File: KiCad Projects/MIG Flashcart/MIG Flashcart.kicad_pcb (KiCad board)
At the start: 4 copper layers, 27.4 x 17 mm, 35 parts, among them J1 Conn_02x04_Counter_Clockwise, J2 Conn_01x17, J3 1040310811, SW1 EVQ-P7A01P, U1 ICE40UP5K-SG48ITR, U2 ESP32-S2, U3 TLV70012_SOT353, U4 TLV70025_SOT353, Y1 ECS-400-10-37B2-CKY-TR

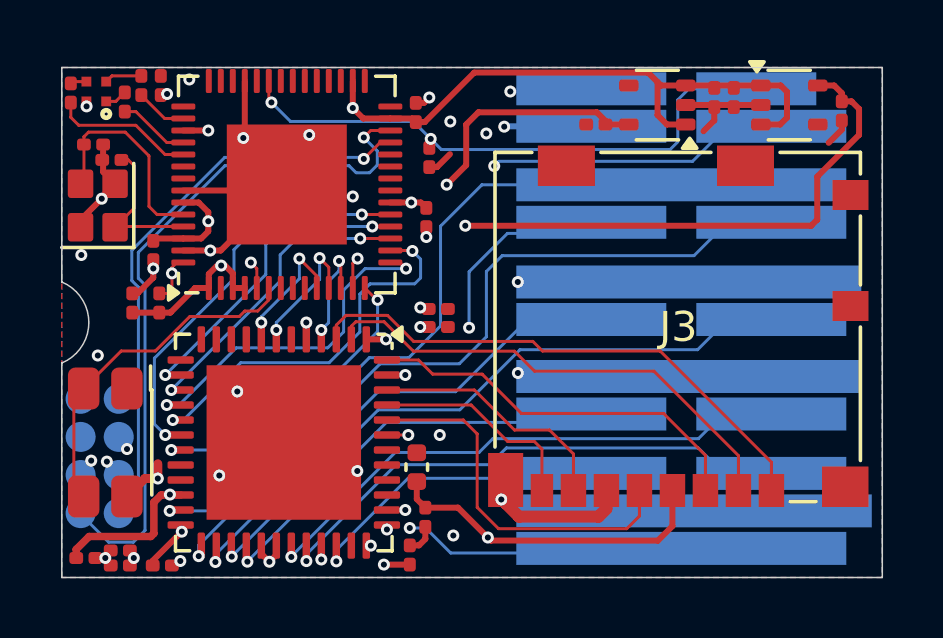
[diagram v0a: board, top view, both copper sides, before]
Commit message: Updated Flashcart PCB, uploaded Flashcart BOM
Revised the Flashcart PCB to the newer revision of the MIG v2, as well as added DigiKey and Mouser BOMs for the Flashcart. One capacitor measurement on the Dumper PCB was corrected as well.
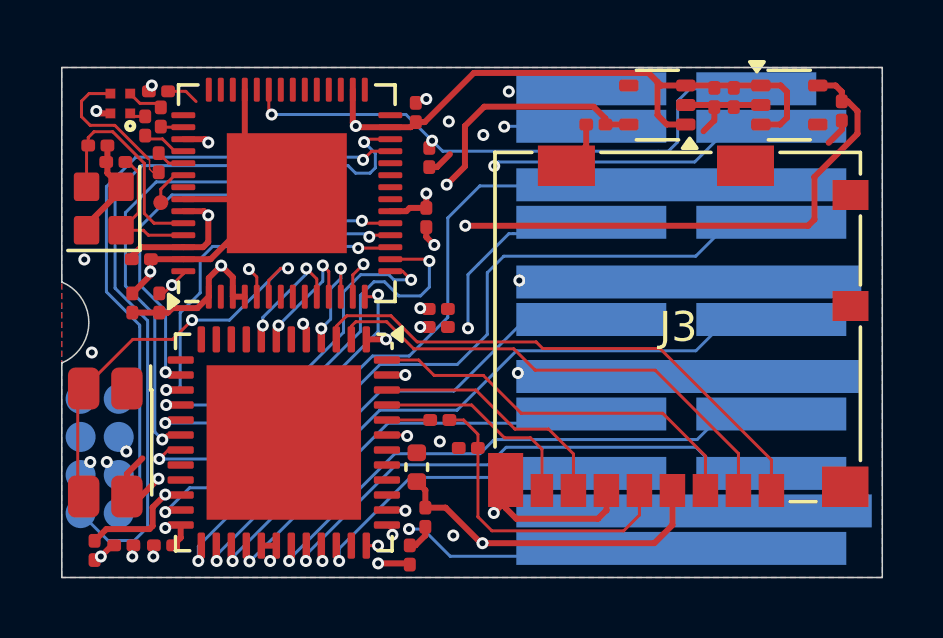
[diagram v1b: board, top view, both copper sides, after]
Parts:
- removed the C5 at (133.9, 112.6)
- added C7: DNP, Capacitor_SMD:C_0201_0603Metric, F.Cu at (145.5, 109.2)
- added R1: 50R, Resistor_SMD:R_0201_0603Metric, F.Cu at (144.6, 108.2)
- added TP1: TestPoint, MIG Flashcart:TestPoint_Pad_D0.5mm, F.Cu at (135.2, 101.0)
- C1, C11, C12, C20, C3, C4, C8, C9: value C -> 0.82u
- C10, C15, C2: value C -> 0.88u
- C16: value 1u -> 0.88u
- C17, C18, C19: value 1u -> 0.82u
- C5: renamed from C6; value C -> 0.82u
- C6: renamed from C7; value C -> 3u3
- moved R3 3.74 mm to (135.2, 99.7), turned to -90 degrees
- moved R6 1.23 mm to (135.2, 98.2)
- moved R5 1.05 mm to (134.7, 98.5)
- moved D1 0.89 mm to (133.9, 97.7)
- moved C2 0.68 mm to (134.0, 112.4)
- moved C3 0.67 mm to (135.3, 112.4), turned to 180 degrees
- moved C11 0.49 mm to (134.6, 102.9), turned to 0 degrees
- moved C1 0.39 mm to (133.0, 112.6), turned to -90 degrees
- moved U2 0.29 mm to (139.4, 100.7)
- moved Y1 0.22 mm to (133.3, 101.2)
- moved C20 0.21 mm to (135.2, 97.3), turned to 0 degrees
- moved C13 0.15 mm to (133.8, 99.7)
- moved C14 0.15 mm to (133.2, 99.1)
- renumbered R1 to R2, R2 to R4, R4 to R5, R5 to R6
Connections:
- J3 pad 5: IOB_3b -> Net-(J3-CLK)
- U1 pad 42: unconnected-(U1A-IOT_51a-Pad42) -> GND
- U2 pad 48: unconnected-(U2-U0TXD-Pad48) -> Net-(U2-U0TXD)
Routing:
- net IOB_3b: track 12.4 -> 1.44 mm
- net Net-(J3-CLK): track 0.00 -> 10.5 mm
- net GND: track 35.0 -> 44.1 mm, vias 23 -> 14
- net VCC: track 122.0 -> 116.1 mm
- net +1V8: track 18.5 -> 12.7 mm
- net GPIO14: track 13.1 -> 18.6 mm
- net Net-(D1-BK): track 0.54 -> 5.11 mm
- net GPIO13: track 10.7 -> 14.6 mm
- net MTMS: track 4.76 -> 0.96 mm
- net GPIO19: track 19.3 -> 21.7 mm
- net GPIO20: track 23.4 -> 25.6 mm
- net GPIO1: track 11.7 -> 13.6 mm, vias 0 -> 2
- net CHIP_PU: track 9.66 -> 8.12 mm
- net +1V2: track 40.6 -> 39.2 mm
- net Net-(U2-U0TXD): track 0.00 -> 1.39 mm
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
